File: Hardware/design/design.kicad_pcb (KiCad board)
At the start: 2 copper layers, 285.8 x 76.2 mm, 69 parts, among them SW1 NKK_NR01, SW10 NKK_NR01, SW11 SW_Push, SW12 SW_Push, SW13 SW_Push, SW14 SW_Push, SW15 NKK_NR01, SW16 SW_Push, SW17 SW_Push, SW18 SW_Push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

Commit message: changed from 4x3 rotary swithches to 2x6 rotary switches for octave control of each half of keyboard
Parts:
- removed SW15, SW20: NKK_NR01, Kicad_Akiyuki_Footprint:NR01
- SW1, SW10: value NKK_NR01 -> Alps_SRBV; footprint Kicad_Akiyuki_Footprint:NR01 -> Kicad_Akiyuki_Footprint:ALPS_SRBV
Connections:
- SW1 pad 1: Net-(D5-Pad1) -> /ROW5
- SW1 pad 2: Net-(D3-Pad1) -> Net-(D5-Pad1)
- SW1 pad 3: /ROW5 -> Net-(D3-Pad1)
- SW1 pad 5: (no net) -> Net-(D7-Pad1)
- SW1 pad 6: (no net) -> Net-(D9-Pad1)
- SW10 pad 1: Net-(D6-Pad1) -> /ROW6
- SW10 pad 2: Net-(D4-Pad1) -> Net-(D6-Pad1)
- SW10 pad 3: /ROW4 -> Net-(D4-Pad1)
- SW10 pad 5: (no net) -> Net-(D12-Pad1)
- SW10 pad 6: (no net) -> Net-(D10-Pad1)

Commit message: added mounting holes, rounded edges and silkscreen
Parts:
- added H1: MountingHole, MountingHole:MountingHole_4mm, F.Cu at (280.7, -3.81)
- added H2: MountingHole, MountingHole:MountingHole_4mm, F.Cu at (5.08, -3.81)
- added H3: MountingHole, MountingHole:MountingHole_4mm, F.Cu at (280.7, 71.1)
- added H4: MountingHole, MountingHole:MountingHole_4mm, F.Cu at (5.08, 71.1)
- moved D6 112.3 mm to (168.1, 13.5), turned to 180 degrees
- moved D4 92.6 mm to (168.1, 11.0), turned to 180 degrees
- moved D2 73.3 mm to (168.1, 8.47), turned to 180 degrees
- moved D12 71.1 mm to (168.1, 5.97), turned to 180 degrees
- moved D8 68.2 mm to (198.1, 8.47), turned to 0 degrees
- moved D1 61.9 mm to (220.1, 8.47), turned to 180 degrees
- moved D10 53.9 mm to (198.1, 5.97), turned to 0 degrees
- moved SW10 43.8 mm to (183.1, 11.0), turned to 270 degrees
- moved D3 39.1 mm to (220.1, 11.0), turned to 180 degrees
- moved D11 33.7 mm to (250.1, 8.47), turned to 0 degrees
- moved D7 32.6 mm to (220.1, 5.97), turned to 180 degrees
- moved D9 27.1 mm to (250.1, 5.97), turned to 0 degrees
- moved D5 18.5 mm to (220.1, 13.5), turned to 180 degrees
- moved SW1 11.6 mm to (235.1, 11.0), turned to 270 degrees
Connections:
- SW1 pad 1: /ROW5 -> /ROW4
- SW1 pad 10: /ROW5 -> /ROW4
- SW10 pad 1: /ROW6 -> /ROW5
- SW10 pad 10: /ROW6 -> /ROW5
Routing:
- net /ROW4: track 29.3 -> 233.0 mm, vias 1 -> 2
- net /ROW5: track 28.5 -> 181.5 mm, vias 1 -> 2
- net /COL5: track 304.9 -> 439.2 mm, vias 5 -> 7
- net /COL2: track 310.0 -> 444.3 mm, vias 11 -> 16
- net /COL3: track 325.4 -> 444.0 mm, vias 8 -> 11
- net /COL0: track 315.0 -> 430.2 mm, vias 7 -> 10
- net /COL4: track 310.7 -> 425.8 mm
- net /COL1: track 292.3 -> 398.5 mm, vias 8 -> 13
- net Net-(D9-Pad1): track 0.00 -> 4.45 mm
- net Net-(D8-Pad1): track 0.00 -> 4.45 mm
- net Net-(D7-Pad1): track 0.00 -> 4.45 mm
- net Net-(D6-Pad1): track 0.00 -> 4.45 mm
- net Net-(D5-Pad1): track 0.00 -> 4.45 mm
- net Net-(D4-Pad1): track 0.00 -> 4.45 mm
- net Net-(D3-Pad1): track 0.00 -> 4.45 mm
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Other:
- board size 285.8 x 76.2 mm -> 285.8 x 85.1 mm
- board text added: "By: Alex"
- board text added: "Left Hand"
- board text added: "MIDI_keyboard V1"
- board text added: "PROMICRO"
- board text added: "Right Hand"
- board text added: "pot0"
- board text added: "pot1"
- board text added: "pot2"
- board text added: "pot3"

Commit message: library management
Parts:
- moved D14 55.0 mm to (101.6, 96.6)
- moved D16 55.0 mm to (234.9, 96.6)
- moved D17 55.0 mm to (44.5, 96.6)
- moved D19 55.0 mm to (177.8, 96.6)
- moved D22 55.0 mm to (120.7, 96.6)
- moved D24 55.0 mm to (254.0, 96.6)
- moved D25 55.0 mm to (63.5, 96.6)
- moved D27 55.0 mm to (196.8, 96.6)
- moved D30 55.0 mm to (139.7, 96.6)
- moved D32 55.0 mm to (273.1, 96.6)
- moved SW12 55.0 mm to (113.7, 96.6)
- moved SW14 55.0 mm to (247.0, 96.6)
- moved SW16 55.0 mm to (56.5, 96.6)
- moved SW17 55.0 mm to (189.8, 96.6)
- moved SW23 55.0 mm to (132.7, 96.6)
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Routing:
- net /COL3: track 444.0 -> 447.2 mm, vias 11 -> 12
- net /COL1: track 398.5 -> 399.6 mm
- net /COL4: track 425.8 -> 426.4 mm
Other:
- outline, holes or cut-outs redrawn

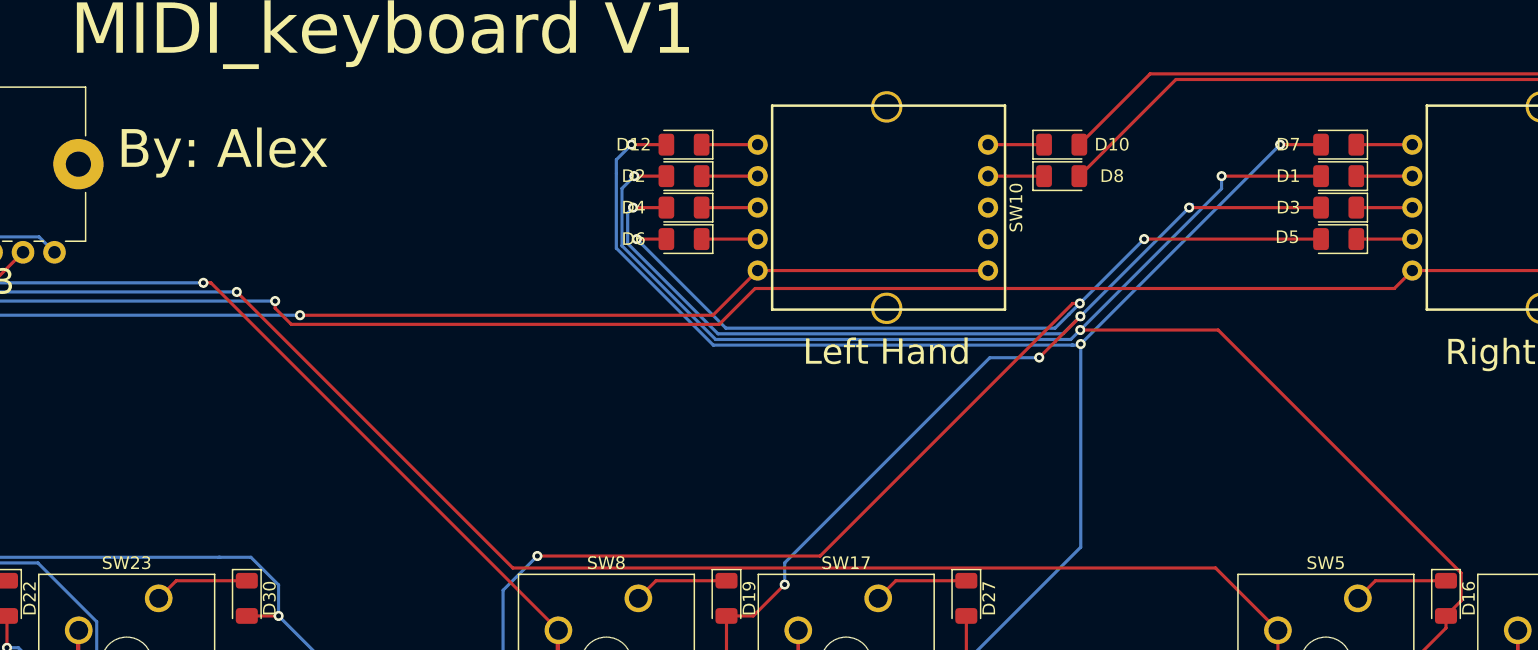
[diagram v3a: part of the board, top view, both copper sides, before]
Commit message: switched COL0 and COL2 positions on the rotary switches
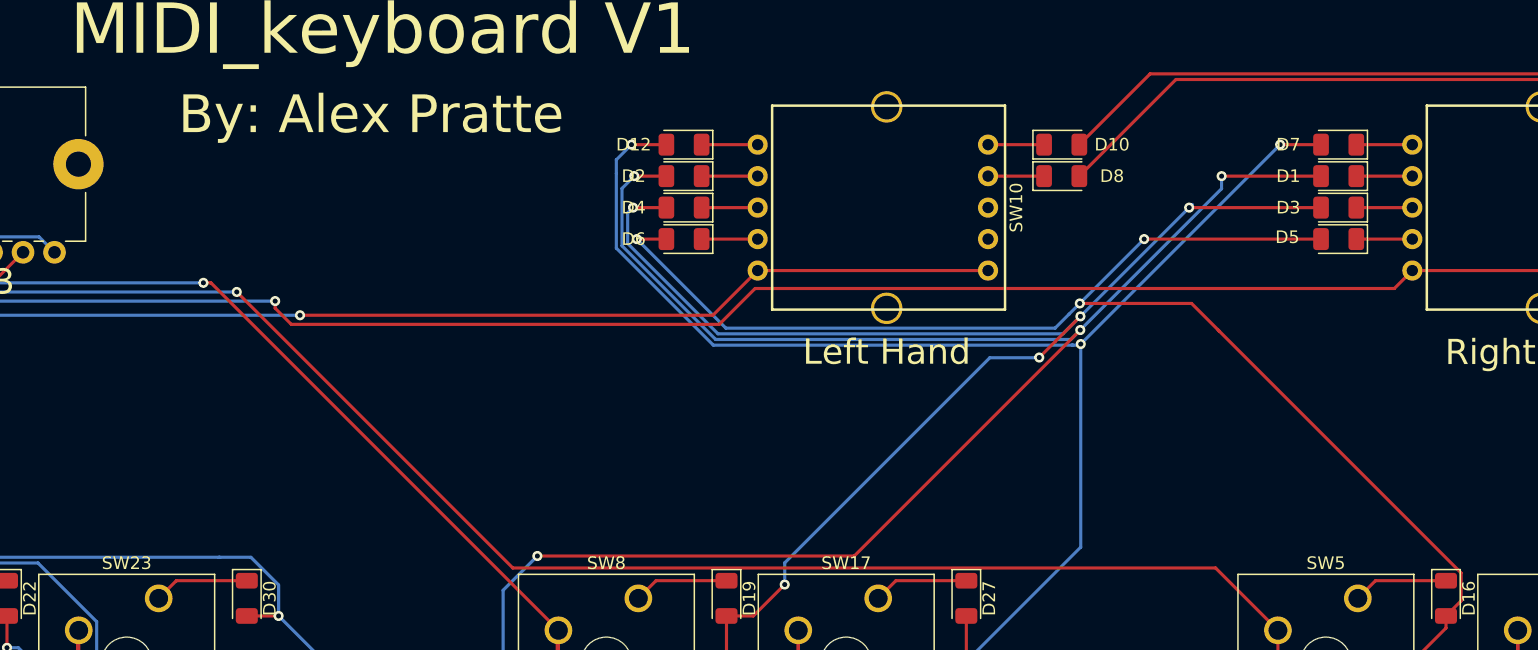
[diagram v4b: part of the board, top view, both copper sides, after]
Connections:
- D1 pad 2: /COL0 -> /COL2
- D2 pad 2: /COL0 -> /COL2
- D5 pad 2: /COL2 -> /COL0
- D6 pad 2: /COL2 -> /COL0
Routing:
- net /COL2: track 444.3 -> 453.9 mm
- net /COL0: track 430.2 -> 420.8 mm
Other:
- board text added: "By: Alex Pratte"
- board text removed: "By: Alex"
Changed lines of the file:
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@@
     (thickness 1.6)
     (drawings 21)
-    (tracks 632)
+    (tracks 634)
     (zones 0)
     (modules 71)
@@
     )
     (pad 2 smd roundrect (at 1.4 0 180) (size 1.25 1.75) (layers F.Cu F.Paste F.Mask) (roundrect_rratio 0.2)
-      (net 25 /COL2))
+      (net 27 /COL0))
     (pad 1 smd roundrect (at -1.4 0 180) (size 1.25 1.75) (layers F.Cu F.Paste F.Mask) (roundrect_rratio 0.2)
       (net 39 "Net-(D6-Pad1)"))
@@
     )
     (pad 2 smd roundrect (at 1.4 0 180) (size 1.25 1.75) (layers F.Cu F.Paste F.Mask) (roundrect_rratio 0.2)
-      (net 25 /COL2))
+      (net 27 /COL0))
     (pad 1 smd roundrect (at -1.4 0 180) (size 1.25 1.75) (layers F.Cu F.Paste F.Mask) (roundrect_rratio 0.2)
       (net 38 "Net-(D5-Pad1)"))
@@
     )
     (pad 2 smd roundrect (at 1.4 0 180) (size 1.25 1.75) (layers F.Cu F.Paste F.Mask) (roundrect_rratio 0.2)
-      (net 27 /COL0))
+      (net 25 /COL2))
     (pad 1 smd roundrect (at -1.4 0 180) (size 1.25 1.75) (layers F.Cu F.Paste F.Mask) (roundrect_rratio 0.2)
       (net 35 "Net-(D2-Pad1)"))
@@
     )
     (pad 2 smd roundrect (at 1.4 0 180) (size 1.25 1.75) (layers F.Cu F.Paste F.Mask) (roundrect_rratio 0.2)
-      (net 27 /COL0))
+      (net 25 /COL2))
     (pad 1 smd roundrect (at -1.4 0 180) (size 1.25 1.75) (layers F.Cu F.Paste F.Mask) (roundrect_rratio 0.2)
       (net 34 "Net-(D1-Pad1)"))
@@
     (effects (font (size 2 2) (thickness 0.15)))
   )
-  (gr_text "By: Alex" (at 137.795 60.96) (layer F.SilkS)
+  (gr_text "By: Alex Pratte" (at 149.575 58.2) (layer F.SilkS)
     (effects (font (size 3 3) (thickness 0.25)))
   )
@@
   (segment (start 46.09499 94.26999) (end 49.074492 97.249492) (width 0.25) (layer F.Cu) (net 25))
   (segment (start 23.375 82.11) (end 35.53499 94.26999) (width 0.25) (layer F.Cu) (net 25))
-  (segment (start 225.025 68.085) (end 210.975 68.085) (width 0.25) (layer F.Cu) (net 25))
-  (segment (start 210.975 68.085) (end 210.975 68.085) (width 0.25) (layer F.Cu) (net 25))
-  (via (at 210.975 68.085) (size 0.8) (drill 0.4) (layers F.Cu B.Cu) (net 25))
-  (segment (start 173.025 68.085) (end 170.675 68.085) (width 0.25) (layer F.Cu) (net 25))
-  (segment (start 170.675 68.085) (end 170.675 68.085) (width 0.25) (layer F.Cu) (net 25))
-  (via (at 170.675 68.085) (size 0.8) (drill 0.4) (layers F.Cu B.Cu) (net 25))
-  (segment (start 203.899999 75.160001) (end 205.0125 74.0475) (width 0.25) (layer B.Cu) (net 25))
-  (segment (start 177.750001 75.160001) (end 203.899999 75.160001) (width 0.25) (layer B.Cu) (net 25))
-  (segment (start 170.675 68.085) (end 177.750001 75.160001) (width 0.25) (layer B.Cu) (net 25))
-  (segment (start 205.0125 74.0475) (end 205.8625 73.1975) (width 0.25) (layer B.Cu) (net 25))
-  (segment (start 205.8625 73.1975) (end 210.975 68.085) (width 0.25) (layer B.Cu) (net 25))
-  (via (at 205.8625 73.1975) (size 0.8) (drill 0.4) (layers F.Cu B.Cu) (net 25))
-  (segment (start 205.296815 73.1975) (end 185.234315 93.26) (width 0.25) (layer F.Cu) (net 25))
-  (segment (start 205.8625 73.1975) (end 205.296815 73.1975) (width 0.25) (layer F.Cu) (net 25))
-  (segment (start 185.234315 93.26) (end 162.775 93.26) (width 0.25) (layer F.Cu) (net 25))
+  (segment (start 225.025 68.085) (end 210.975 68.085) (width 0.25) (layer F.Cu) (net 27))
+  (segment (start 210.975 68.085) (end 210.975 68.085) (width 0.25) (layer F.Cu) (net 27))
+  (via (at 210.975 68.085) (size 0.8) (drill 0.4) (layers F.Cu B.Cu) (net 27))
+  (segment (start 173.025 68.085) (end 170.675 68.085) (width 0.25) (layer F.Cu) (net 27))
+  (segment (start 170.675 68.085) (end 170.675 68.085) (width 0.25) (layer F.Cu) (net 27))
+  (via (at 170.675 68.085) (size 0.8) (drill 0.4) (layers F.Cu B.Cu) (net 27))
+  (segment (start 203.899999 75.160001) (end 205.0125 74.0475) (width 0.25) (layer B.Cu) (net 27))
+  (segment (start 177.750001 75.160001) (end 203.899999 75.160001) (width 0.25) (layer B.Cu) (net 27))
+  (segment (start 170.675 68.085) (end 177.750001 75.160001) (width 0.25) (layer B.Cu) (net 27))
+  (segment (start 205.0125 74.0475) (end 205.8625 73.1975) (width 0.25) (layer B.Cu) (net 27))
+  (segment (start 205.8625 73.1975) (end 210.975 68.085) (width 0.25) (layer B.Cu) (net 27))
+  (via (at 205.8625 73.1975) (size 0.8) (drill 0.4) (layers F.Cu B.Cu) (net 27))
   (segment (start 162.775 93.26) (end 162.775 93.26) (width 0.25) (layer F.Cu) (net 25))
   (via (at 162.775 93.26) (size 0.8) (drill 0.4) (layers F.Cu B.Cu) (net 25))
@@
   (segment (start 18.295 120.479002) (end 20.890999 123.075001) (width 0.25) (layer F.Cu) (net 27))
   (segment (start 18.295 71.55) (end 18.295 120.479002) (width 0.25) (layer F.Cu) (net 27))
-  (segment (start 225.025 63.085) (end 217.125 63.085) (width 0.25) (layer F.Cu) (net 27))
-  (segment (start 217.125 63.085) (end 217.125 63.085) (width 0.25) (layer F.Cu) (net 27))
-  (via (at 217.125 63.085) (size 0.8) (drill 0.4) (layers F.Cu B.Cu) (net 27))
-  (segment (start 173.025 63.085) (end 170.475 63.085) (width 0.25) (layer F.Cu) (net 27))
-  (segment (start 170.475 63.085) (end 170.475 63.085) (width 0.25) (layer F.Cu) (net 27))
-  (via (at 170.475 63.085) (size 0.8) (drill 0.4) (layers F.Cu B.Cu) (net 27))
-  (segment (start 205.147981 76.060021) (end 205.899001 75.309001) (width 0.25) (layer B.Cu) (net 27))
-  (segment (start 176.940609 76.060021) (end 205.147981 76.060021) (width 0.25) (layer B.Cu) (net 27))
-  (segment (start 217.125 64.083002) (end 217.125 63.085) (width 0.25) (layer B.Cu) (net 27))
-  (segment (start 169.49999 68.619402) (end 176.940609 76.060021) (width 0.25) (layer B.Cu) (net 27))
-  (segment (start 169.49999 64.06001) (end 169.49999 68.619402) (width 0.25) (layer B.Cu) (net 27))
-  (segment (start 170.475 63.085) (end 169.49999 64.06001) (width 0.25) (layer B.Cu) (net 27))
-  (segment (start 205.899001 75.309001) (end 217.125 64.083002) (width 0.25) (layer B.Cu) (net 27))
-  (via (at 205.899001 75.309001) (size 0.8) (drill 0.4) (layers F.Cu B.Cu) (net 27))
+  (segment (start 225.025 63.085) (end 217.125 63.085) (width 0.25) (layer F.Cu) (net 25))
+  (segment (start 217.125 63.085) (end 217.125 63.085) (width 0.25) (layer F.Cu) (net 25))
+  (via (at 217.125 63.085) (size 0.8) (drill 0.4) (layers F.Cu B.Cu) (net 25))
+  (segment (start 173.025 63.085) (end 170.475 63.085) (width 0.25) (layer F.Cu) (net 25))
+  (segment (start 170.475 63.085) (end 170.475 63.085) (width 0.25) (layer F.Cu) (net 25))
+  (via (at 170.475 63.085) (size 0.8) (drill 0.4) (layers F.Cu B.Cu) (net 25))
+  (segment (start 205.147981 76.060021) (end 205.899001 75.309001) (width 0.25) (layer B.Cu) (net 25))
+  (segment (start 176.940609 76.060021) (end 205.147981 76.060021) (width 0.25) (layer B.Cu) (net 25))
+  (segment (start 217.125 64.083002) (end 217.125 63.085) (width 0.25) (layer B.Cu) (net 25))
+  (segment (start 169.49999 68.619402) (end 176.940609 76.060021) (width 0.25) (layer B.Cu) (net 25))
+  (segment (start 169.49999 64.06001) (end 169.49999 68.619402) (width 0.25) (layer B.Cu) (net 25))
+  (segment (start 170.475 63.085) (end 169.49999 64.06001) (width 0.25) (layer B.Cu) (net 25))
+  (segment (start 205.899001 75.309001) (end 217.125 64.083002) (width 0.25) (layer B.Cu) (net 25))
+  (via (at 205.899001 75.309001) (size 0.8) (drill 0.4) (layers F.Cu B.Cu) (net 25))
+  (segment (start 205.897003 75.309001) (end 205.899001 75.309001) (width 0.25) (layer F.Cu) (net 25))
+  (segment (start 187.946004 93.26) (end 205.897003 75.309001) (width 0.25) (layer F.Cu) (net 25))
+  (segment (start 162.775 93.26) (end 187.946004 93.26) (width 0.25) (layer F.Cu) (net 25))
   (segment (start 236.15001 96.81999) (end 234.95 98.02) (width 0.25) (layer F.Cu) (net 27))
   (segment (start 236.15001 94.60682) (end 236.15001 96.81999) (width 0.25) (layer F.Cu) (net 27))
-  (segment (start 216.852191 75.309001) (end 236.15001 94.60682) (width 0.25) (layer F.Cu) (net 27))
-  (segment (start 205.899001 75.309001) (end 216.852191 75.309001) (width 0.25) (layer F.Cu) (net 27))
+  (segment (start 214.74069 73.1975) (end 216.959095 75.415905) (width 0.25) (layer F.Cu) (net 27))
+  (segment (start 205.8625 73.1975) (end 214.74069 73.1975) (width 0.25) (layer F.Cu) (net 27))
+  (segment (start 216.959095 75.415905) (end 236.15001 94.60682) (width 0.25) (layer F.Cu) (net 27))
+  (segment (start 216.852191 75.309001) (end 216.959095 75.415905) (width 0.25) (layer F.Cu) (net 27))
   (segment (start 57.9 95.22) (end 56.5 96.62) (width 0.25) (layer F.Cu) (net 28))
   (segment (start 63.5 95.22) (end 57.9 95.22) (width 0.25) (layer F.Cu) (net 28))
